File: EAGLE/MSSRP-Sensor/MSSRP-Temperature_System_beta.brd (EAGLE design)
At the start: 100 x 100 mm, 225 parts, among them J1 POWER_JACKPTH, J10 BNCPTH, J11 BNCPTH, J2 USBSMD, J4 TE-2-TERMBLOCK, J5 TE-2-TERMBLOCK, J6 TE-2-TERMBLOCK, J7 TE-2-TERMBLOCK, J8 BNCPTH, J9 BNCPTH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

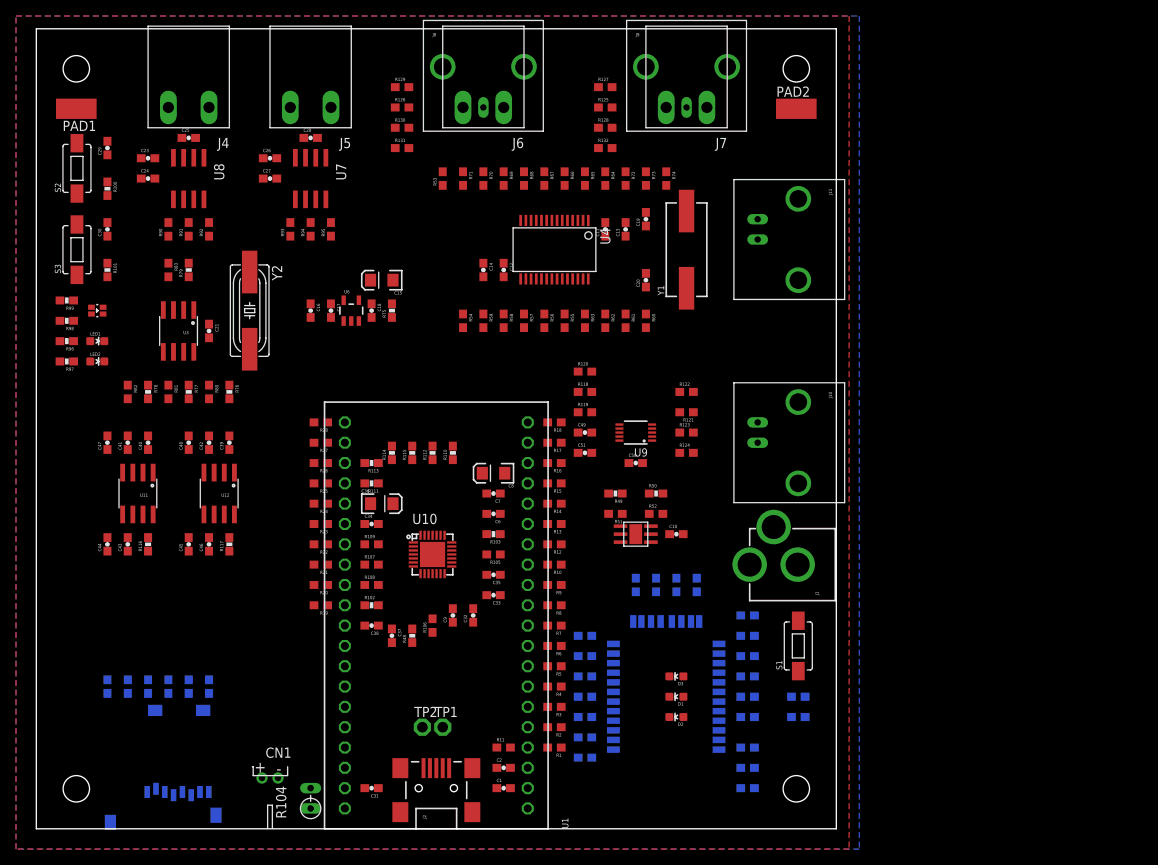
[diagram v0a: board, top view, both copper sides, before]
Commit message: Layout start
Some schematic changes, eliminating several 0-ohm “oops” resistors.
General layout OK, initial routing started.
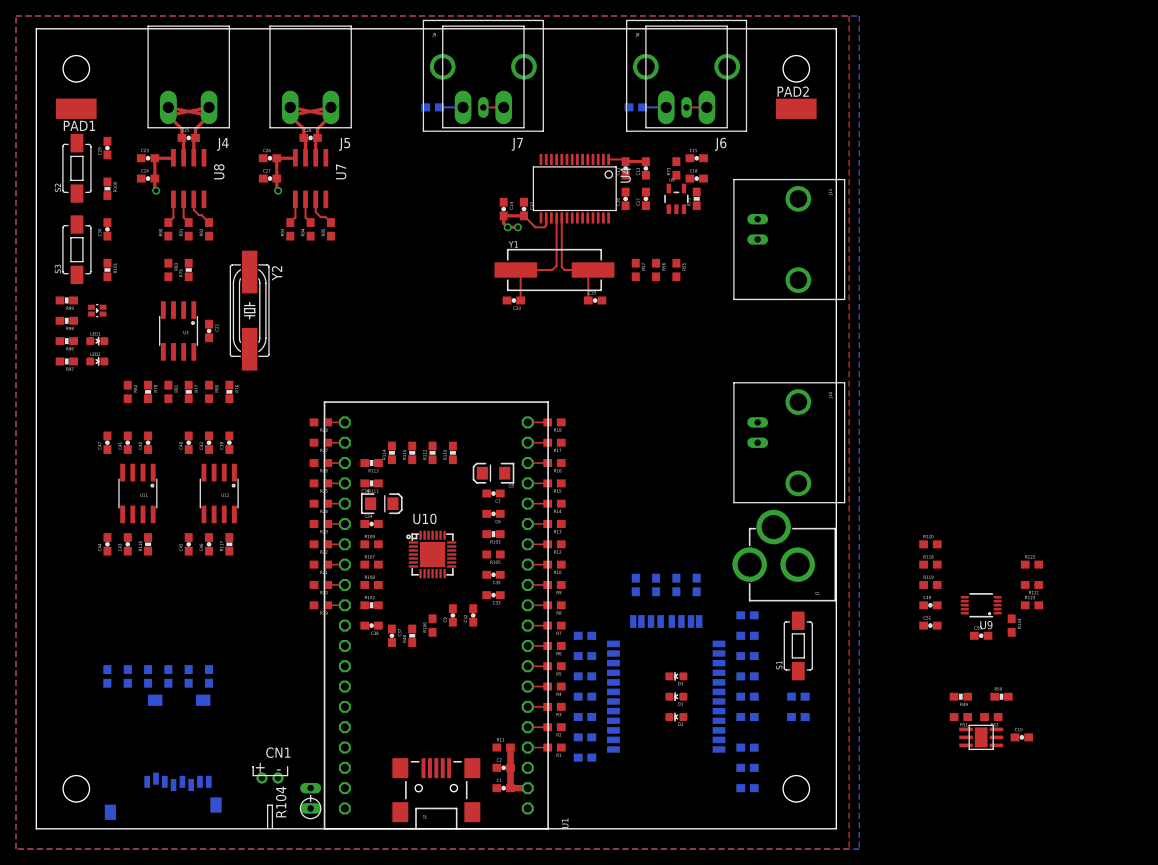
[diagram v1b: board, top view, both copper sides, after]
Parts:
- removed C31: 0.1uF, SparkFun-Capacitors:0603-CAP
- removed R125, R126, R127, R129, R131, R132, R53, R54, R58, R59, R60, R61, R62, R63, R64, R65, R66, R67, R68, R69, R70, R71, R72, R74: 0, SparkFun-Resistors:0603
- removed TP1, TP2: TPPAD1-13, testpad:P1-13
- C15: value 10uF -> 4.7uF; device SparkFun-Capacitors:EIA3216 -> SparkFun-Capacitors:0603-CAP
- moved R50 50.1 mm to (120.7, 16.5)
- moved C10 50.1 mm to (123.2, 11.4)
- moved R49 50.1 mm to (115.6, 16.5)
- moved R51 50.1 mm to (115.6, 14.0)
- moved U5 50.1 mm to (118.1, 11.4)
- moved R52 49.0 mm to (119.4, 14.0), turned to 180 degrees
- moved C49 48.3 mm to (111.8, 27.9)
- moved C51 48.3 mm to (111.8, 25.4)
- moved R119 48.3 mm to (111.8, 30.5)
- moved R118 48.3 mm to (111.8, 33.0)
- moved R120 48.3 mm to (111.8, 35.6)
- moved C50 48.3 mm to (118.1, 24.1)
- moved R121 48.3 mm to (124.5, 30.5)
- moved R122 48.3 mm to (124.5, 33.0)
- moved R123 48.3 mm to (124.5, 27.9)
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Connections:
- removed net AFE_D0: R63.2
- removed net AFE_D1: R62.2
- removed net AFE_D2: R61.2
- removed net AFE_D3: R60.2
- removed net N$127: J2.D-, TP2.TP
- removed net N$128: J2.D+, TP1.TP
- removed net N$129: J8.S, R126.2
- removed net N$130: J9.S, R125.2
- removed net N$131: J7.1, R127.2
- removed net N$132: J7.2, R128.2
- removed net N$133: J6.1, R129.2
- removed net N$134: J6.2, R130.2
- removed net N$49: R53.1, U4.14
- removed net N$50: R54.1, U4.15
- removed net N$54: R58.1, U4.21
- removed net N$55: R59.1, U4.20
- removed net N$56: R60.1, U4.28
- removed net N$57: R61.1, U4.27
- removed net N$58: R62.1, U4.26
- removed net N$59: R63.1, U4.25
- removed net N$60: R64.2, U4.6
- removed net N$61: R65.2, U4.7
- removed net N$62: R66.2, U4.8
- removed net N$63: R67.2, U4.9
- removed net N$64: R68.2, U4.10
- removed net N$65: R69.2, U4.11
- removed net N$66: R70.2, U4.12
- removed net N$67: R71.2, U4.13
- removed net N$68: R72.2, U4.5
- removed net N$70: R74.2, U4.3
- removed net N$84: R23.2
- net 5V: now also C15.1; no longer C15.A
- net AFE_!DRDY: now also U4.21; no longer R58.2
- net AFE_!PWDN: now also U4.14; no longer R53.2
- net AFE_!RESET: now also R23.2, U4.15; no longer R54.2
- net AFE_AIN0: now also J6.1, J8.S, U4.6; no longer R126.1, R129.1, R64.1
- net AFE_AIN1: now also J6.2, J8.GND, R130.2, U4.7; no longer R130.1, R131.1, R65.1
- net AFE_AIN2: now also J7.1, J9.S, U4.8; no longer R125.1, R127.1, R66.1
- net AFE_AIN3: now also J7.2, J9.GND, R128.2, U4.9; no longer R128.1, R132.1, R67.1
- net CS_AFE: now also U4.20; no longer R59.2
- net GND: now also C15.2, R128.1, R130.1, U4.3, U4.5; no longer C15.C, C31.1, J8.GND, J9.GND, R131.2, R132.2, R68.1, R69.1, R70.1, R71.1, R72.1, R74.1
- net VUSB: no longer C31.2, J2.VBUS, U1.39
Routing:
- net 3.3V: track 0.00 -> 22.8 mm, vias 0 -> 4
- net N$72: track 0.00 -> 15.3 mm
- net N$73: track 0.00 -> 14.0 mm
- net AIN1-: track 0.00 -> 11.2 mm
- net AIN1+: track 0.00 -> 11.2 mm
- net AIN0-: track 0.00 -> 11.2 mm
- net AIN0+: track 0.00 -> 11.2 mm
- net N$8: track 0.00 -> 7.24 mm
- net 5V: track 0.00 -> 4.78 mm
- net N$89: track 0.00 -> 4.04 mm
- net N$86: track 0.00 -> 3.89 mm
- net N$87: track 0.00 -> 3.16 mm
- net N$91: track 0.00 -> 3.16 mm
- net N$90: track 0.00 -> 3.16 mm
- net N$88: track 0.00 -> 3.16 mm
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
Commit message: Updated routing
Schematic and routing edits. Core power routing done.
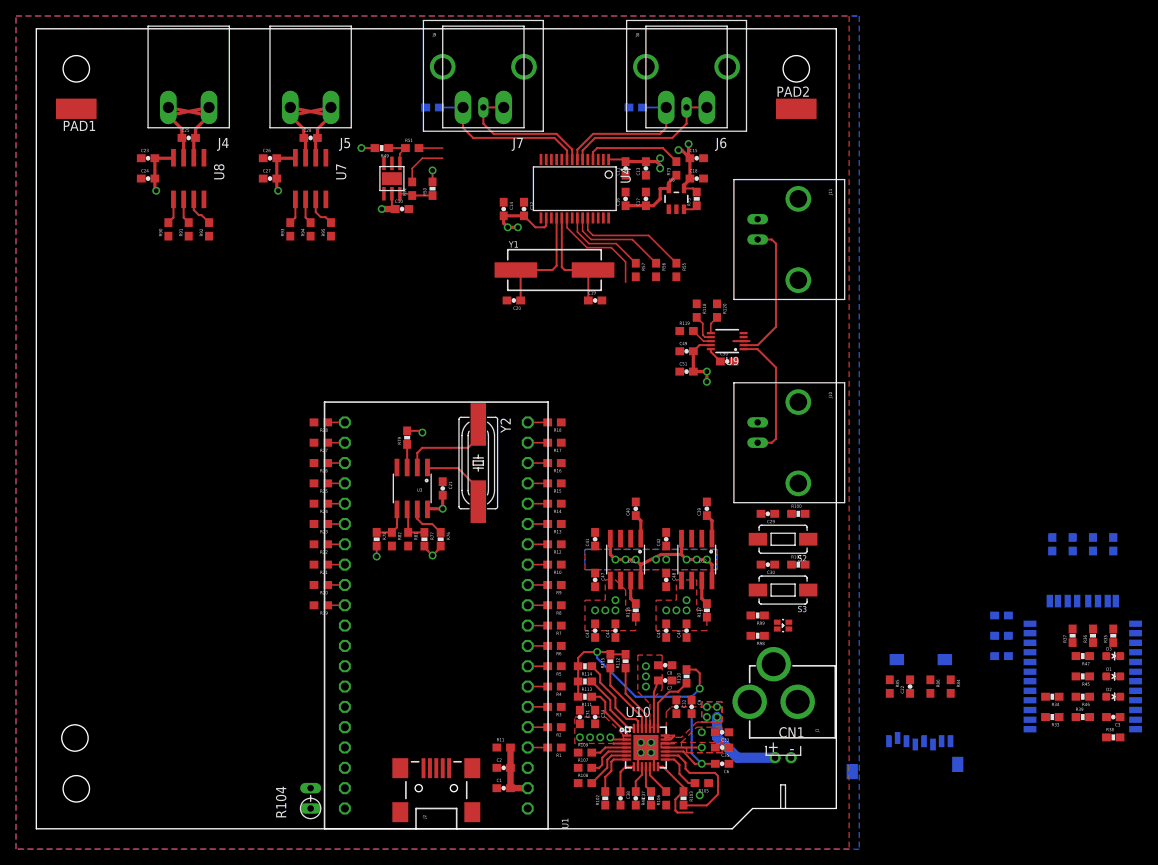
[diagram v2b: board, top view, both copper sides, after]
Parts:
- removed C36: 10uF, SparkFun-Capacitors:EIA3216
- removed LED1, LED2: (no value), SparkFun-LED:LED-0603
- removed R121, R122, R123, R124, R29, R30, R31, R32, R80, R83, R87, R89: 0, SparkFun-Resistors:0603
- removed R96, R97: 470, SparkFun-Resistors:0603-RES
- removed S1: SWITCH-MOMENTARY-2-SMD-1101NE, SparkFun-Electromechanical:TACTILE-SWITCH-1101NE
- added C31: 4.7uF, SparkFun-Capacitors:0603-CAP
- C8: value 10uF -> 4.7uF; device SparkFun-Capacitors:EIA3216 -> SparkFun-Capacitors:0603-CAP
- moved C10 101.8 mm to (45.7, 77.5)
- moved U5 101.5 mm to (44.5, 81.3), turned to 270 degrees
- moved R49 99.7 mm to (43.2, 85.1)
- moved S2 99.7 mm to (93.3, 36.2), turned to 180 degrees
- moved R51 98.8 mm to (47.0, 85.1), turned to 0 degrees
- moved R52 98.0 mm to (47.0, 80.0), turned to 90 degrees
- moved S3 98.0 mm to (93.3, 29.8), turned to 180 degrees
- moved R100 95.4 mm to (95.2, 39.4), turned to 0 degrees
- moved R50 95.3 mm to (49.5, 80.0), turned to 90 degrees
- moved C22 95.3 mm to (109.2, 17.8), flipped to the top
- moved R84 95.3 mm to (114.3, 17.8), flipped to the top
- moved R85 95.3 mm to (106.7, 17.8), flipped to the top
- moved R86 95.3 mm to (111.8, 17.8), flipped to the top
- moved R98 94.9 mm to (90.2, 24.1)
- moved R99 94.9 mm to (90.2, 26.7)
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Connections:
- net N$108 renamed VBATT
- net N$96 renamed VLDO
- removed net BATT_!CHG: R17.1
- removed net BICOLOR_LED0: R27.2
- removed net BICOLOR_LED1: R28.2
- removed net CS_BT: R30.1, R5.1
- removed net N$122: R121.2, U9.4
- removed net N$123: R122.1, U9.5
- removed net N$125: R123.1, U9.2
- removed net N$126: R124.1, U9.1
- removed net N$29: R29.2, U2.6
- removed net N$31: R31.2, U2.24
- removed net N$32: R32.2, U2.2
- removed net N$38: C3.1, R38.2, S1.P$1, U2.22
- removed net N$76: R76.1, R80.1, U3.7
- removed net N$79: R79.1, R83.2, U3.3
- removed net N$80: R87.2, U$1.2
- removed net N$85: R89.2, U$1.CD1
- removed net N$94: LED1.A, R96.1
- removed net N$95: LED2.A, R97.1
- removed net SQW: R20.2
- removed net STATUS_CONN: R96.2
- removed net STATUS_PWR: R26.2, R97.2
- removed net SW1: C29.1, R100.1, R24.2, S2.P$2
- new net BT_!RESET: C3.1, R38.2, R5.1, U2.22
- new net LED0: R27.2, R98.2
- new net LED1: R28.2, R99.2
- net 3.3V: no longer S1.P$2
- net CS_SD: now also U$1.2; no longer R87.1
- net DAC0: now also U9.1; no longer R124.2
- net DAC1: now also U9.2; no longer R123.2
- net DAC_!CLR: now also R26.2, U9.5; no longer R122.2
- net DAC_!LDAC: now also R17.1, U9.4; no longer R121.1
- net GND: now also C31.1, C8.1; no longer C36.C, C8.C, LED1.C, LED2.C
- net MICRO_!RESET: now also C29.1, R100.1, S2.P$2
- net MISO: no longer R31.1
- net MOSI: no longer R32.1
- net N$30: now also R24.2; no longer R30.2, U2.23
- net N$5: no longer R98.2
- net N$6: no longer R99.2
- net RTC_!INTA: now also R79.1, U3.3; no longer R83.1
- net RTC_SQW: now also R20.2, R76.1, U3.7; no longer R80.2
- net SCK: no longer R29.1
- net SD_CD: now also U$1.CD1; no longer R89.1
- net VIN: now also C31.2; no longer C36.A
- net VSYS: now also C8.2; no longer C8.A
- net VUSB: now also U1.39
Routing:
- net VLDO: track 0.00 -> 46.9 mm, vias 0 -> 3
- net VSYS: track 0.00 -> 29.0 mm, vias 0 -> 11
- net 5V: track 4.78 -> 25.3 mm, vias 0 -> 10
- net DAC1: track 0.00 -> 17.9 mm
- net AFE_AIN3: track 2.96 -> 20.8 mm
- net AFE_AIN0: track 2.54 -> 20.1 mm
- net 3.3V: track 22.8 -> 39.9 mm, vias 4 -> 15
- net DAC0: track 0.00 -> 16.4 mm
- net AFE_AIN1: track 2.96 -> 19.0 mm
- net AFE_AIN2: track 2.54 -> 18.3 mm
- net N$98: track 0.00 -> 15.3 mm
- net VBATT: track 0.00 -> 14.7 mm, vias 0 -> 4
- net N$51: track 0.00 -> 14.3 mm
- net CS_AFE: track 0.00 -> 12.8 mm
- net N$52: track 0.00 -> 12.5 mm
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- added copper zone on layer 1, net 3.3V
- added copper zone on layer 1, net 5V
- added copper zone on layer 1, net VBATT
- added copper zone on layer 16, net VBATT
- added copper zone on layer 1, net VIN
- added copper zone on layer 1, net VSYS
- added copper zone on layer 16, net VSYS
- added copper zone on layer 1, net VUSB
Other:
- outline, holes or cut-outs redrawn
